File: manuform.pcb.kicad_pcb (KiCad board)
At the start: 2 copper layers, 84.5 x 93.5 mm, 100 parts, among them J1 Conn_01x01_Pin, J10 Conn_01x01_Pin, J11 Conn_01x01_Pin, J12 Conn_01x01_Pin, J2 Conn_01x01_Pin, J3 Conn_01x01, J4 Conn_01x01, J5 Conn_01x01_Pin, J6 Conn_01x01_Pin, J7 Conn_01x01_Pin, J8 Conn_01x01_Pin, J9 Conn_01x01_Pin, SW1 SW_DIP_x01, SW2 SW_DIP_x01, SW3 SW_DIP_x01, SW4 SW_DIP_x01

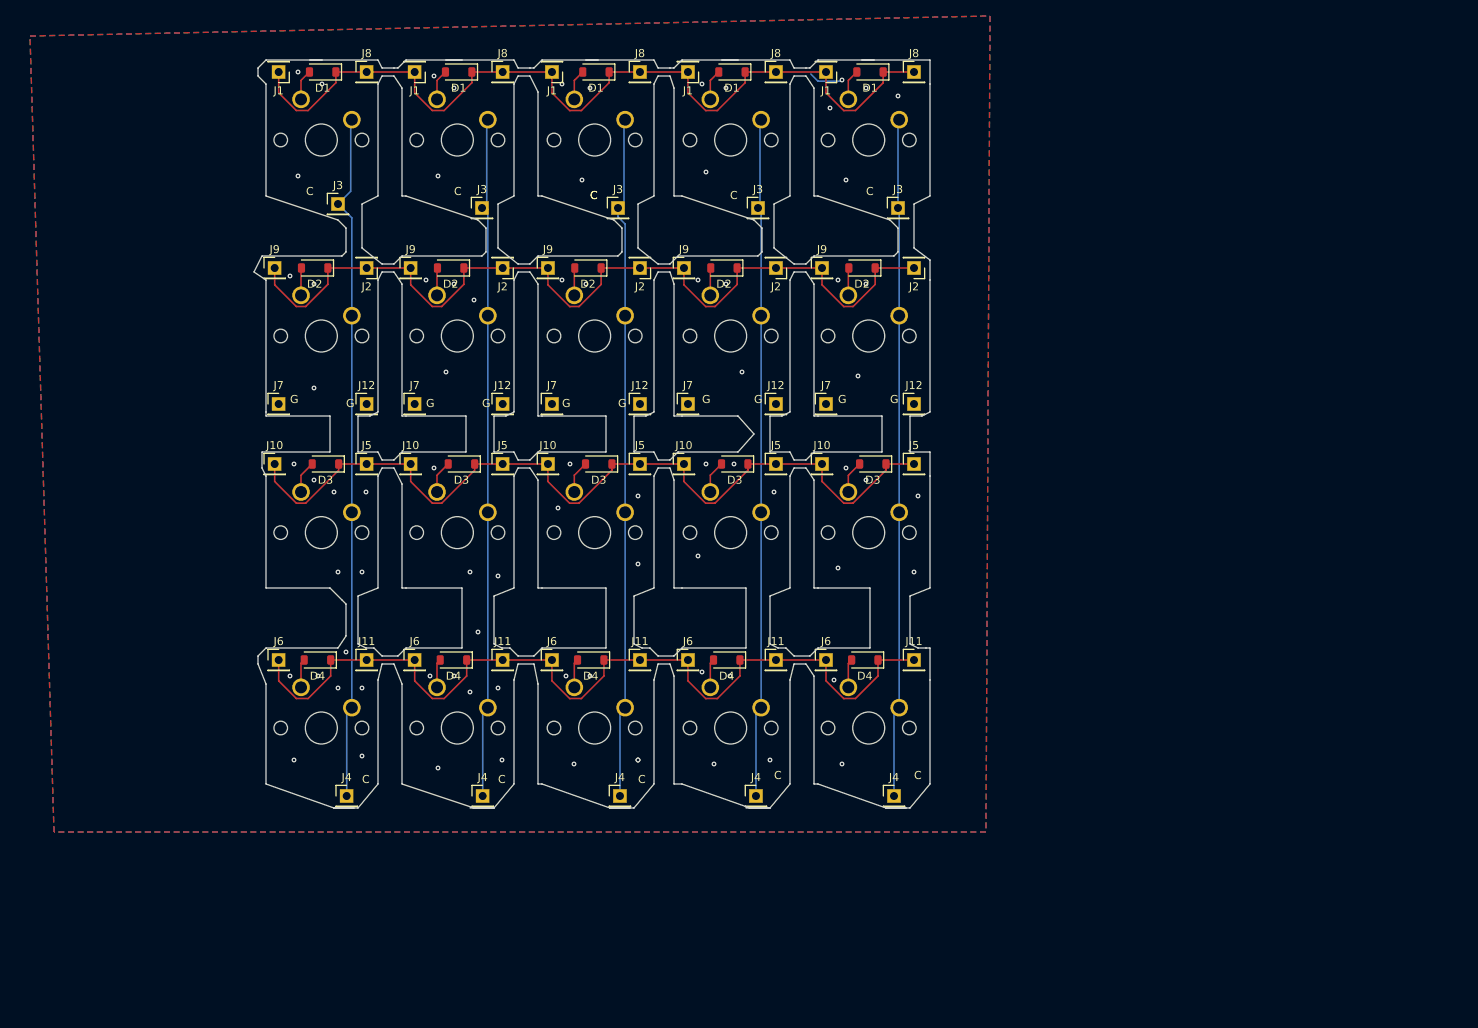
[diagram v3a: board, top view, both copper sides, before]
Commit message: new version with longer mehanical and solder holes.
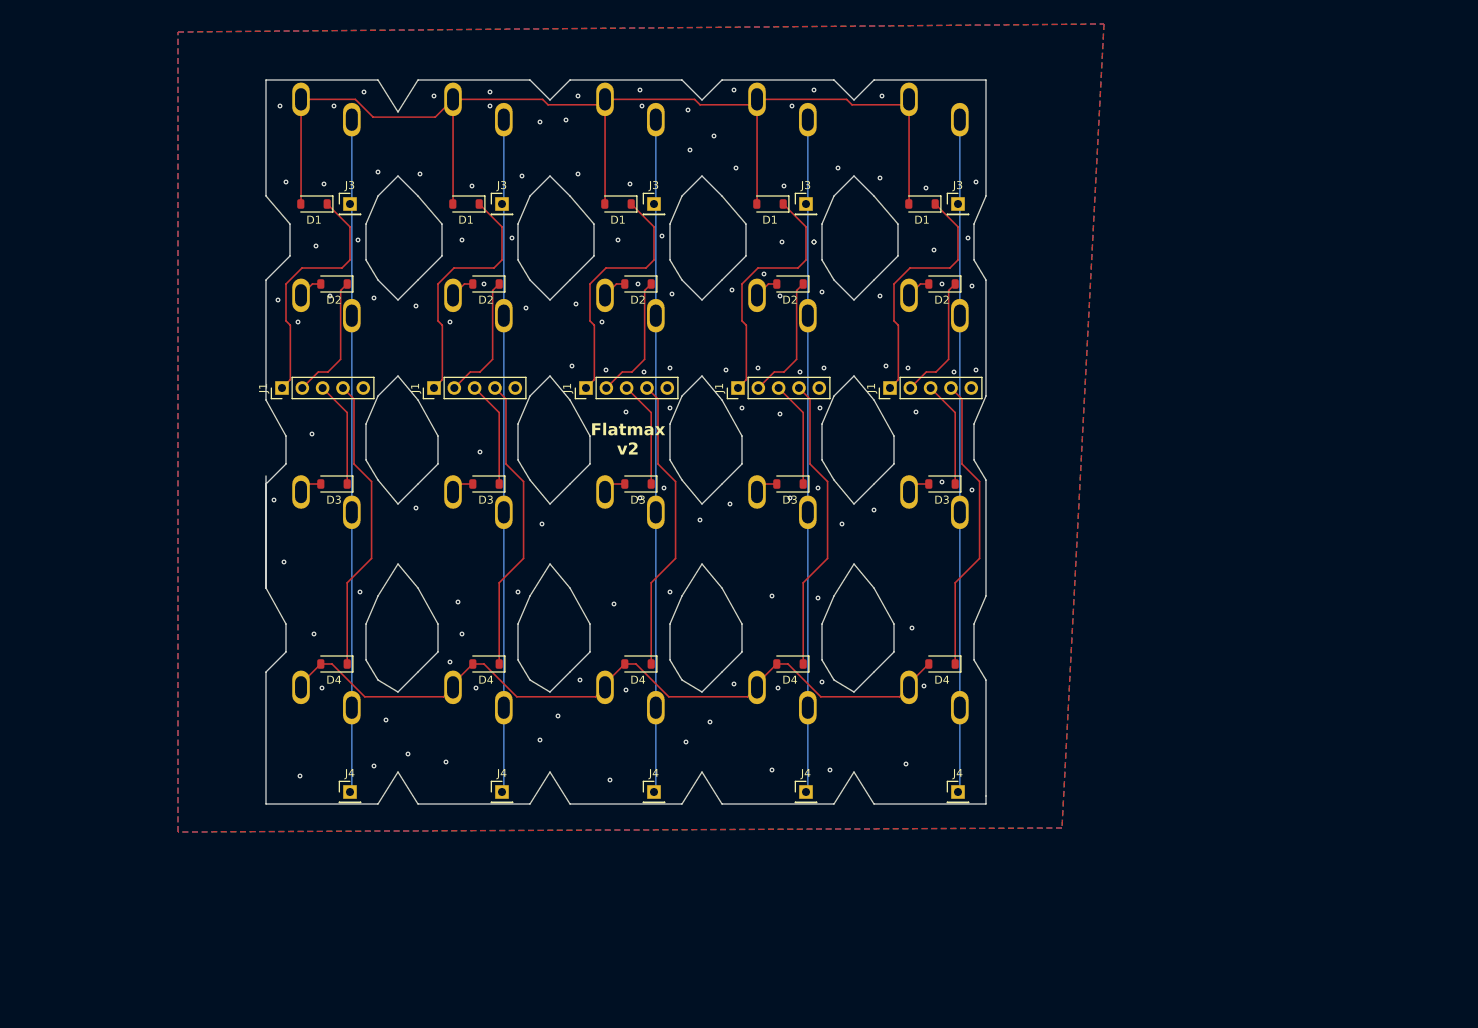
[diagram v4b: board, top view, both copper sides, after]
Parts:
- removed the D1 at (139.1, 16.5)
- removed the D1 at (156.2, 16.5)
- removed the D1 at (190.5, 16.5)
- removed the D1 at (173.2, 16.5)
- removed the D2 at (172.2, 41.0)
- removed the D2 at (138.1, 41.0)
- removed the D2 at (155.2, 41.0)
- removed the D2 at (189.5, 41.0)
- removed the D3 at (173.6, 65.5)
- removed the D3 at (139.4, 65.5)
- removed the D3 at (190.8, 65.5)
- removed the D3 at (156.6, 65.5)
- removed the D4 at (172.6, 90.0)
- removed the D4 at (138.4, 90.0)
- removed the D4 at (155.6, 90.0)
- removed the D4 at (189.8, 90.0)
- removed the J1 at (150.7, 16.5)
- removed the J1 at (185.0, 16.5)
- removed the J1 at (167.7, 16.5)
- removed the J1 at (133.6, 16.5)
- removed J10 (x5), J11 (x5), J12 (x5), J2 (x5), J5 (x5), J6 (x5), J7 (x5), J8 (x5), J9 (x5): Conn_01x01_Pin, Connector_PinHeader_2.54mm:PinHeader_1x01_P2.54mm_Vertical
- removed the J3 at (159.0, 33.5)
- removed the J3 at (142.0, 33.5)
- removed the J3 at (176.5, 33.5)
- removed the J3 at (194.0, 33.5)
- removed the J4 at (176.2, 107.0)
- removed the J4 at (159.2, 107.0)
- removed the J4 at (142.1, 107.0)
- removed the J4 at (193.5, 107.0)
- removed the SW1 at (153.5, 19.9)
- removed the SW1 at (136.4, 19.9)
- removed the SW1 at (187.8, 19.9)
- removed the SW1 at (170.5, 19.9)
- removed the SW2 at (136.4, 44.4)
- removed the SW2 at (170.5, 44.4)
- removed the SW2 at (187.8, 44.4)
- removed the SW2 at (153.5, 44.4)
- removed the SW3 at (187.8, 69.0)
- removed the SW3 at (136.4, 69.0)
- removed the SW3 at (170.5, 69.0)
- removed the SW3 at (153.5, 69.0)
- removed the SW4 at (170.5, 93.4)
- removed the SW4 at (153.5, 93.4)
- removed the SW4 at (187.8, 93.4)
- removed the SW4 at (136.4, 93.4)
- added D1: D, Diode_SMD:D_SOD-123, F.Cu at (178.0, 33.0)
- added D1: D, Diode_SMD:D_SOD-123, F.Cu at (159.0, 33.0)
- added D1: D, Diode_SMD:D_SOD-123, F.Cu at (197.0, 33.0)
- added D1: D, Diode_SMD:D_SOD-123, F.Cu at (140.0, 33.0)
- added D2: D, Diode_SMD:D_SOD-123, F.Cu at (199.5, 43.0)
- added D2: D, Diode_SMD:D_SOD-123, F.Cu at (142.5, 43.0)
- added D2: D, Diode_SMD:D_SOD-123, F.Cu at (180.5, 43.0)
- added D2: D, Diode_SMD:D_SOD-123, F.Cu at (161.5, 43.0)
- added D3: D, Diode_SMD:D_SOD-123, F.Cu at (199.5, 68.0)
- added D3: D, Diode_SMD:D_SOD-123, F.Cu at (180.5, 68.0)
- added D3: D, Diode_SMD:D_SOD-123, F.Cu at (142.5, 68.0)
- added D3: D, Diode_SMD:D_SOD-123, F.Cu at (161.5, 68.0)
- added D4: D, Diode_SMD:D_SOD-123, F.Cu at (199.5, 90.5)
- added D4: D, Diode_SMD:D_SOD-123, F.Cu at (180.5, 90.5)
- added D4: D, Diode_SMD:D_SOD-123, F.Cu at (142.5, 90.5)
- added D4: D, Diode_SMD:D_SOD-123, F.Cu at (161.5, 90.5)
- added J1: Conn_01x05, Connector_PinHeader_2.54mm:PinHeader_1x05_P2.54mm_Vertical, F.Cu at (193.0, 56.0)
- added J1: Conn_01x05, Connector_PinHeader_2.54mm:PinHeader_1x05_P2.54mm_Vertical, F.Cu at (155.0, 56.0)
- added J1: Conn_01x05, Connector_PinHeader_2.54mm:PinHeader_1x05_P2.54mm_Vertical, F.Cu at (136.0, 56.0)
- added J1: Conn_01x05, Connector_PinHeader_2.54mm:PinHeader_1x05_P2.54mm_Vertical, F.Cu at (174.0, 56.0)
- added J3: Conn_01x01, Connector_PinHeader_2.54mm:PinHeader_1x01_P2.54mm_Vertical, F.Cu at (163.5, 33.0)
- added J3: Conn_01x01, Connector_PinHeader_2.54mm:PinHeader_1x01_P2.54mm_Vertical, F.Cu at (182.5, 33.0)
- added J3: Conn_01x01, Connector_PinHeader_2.54mm:PinHeader_1x01_P2.54mm_Vertical, F.Cu at (144.5, 33.0)
- added J3: Conn_01x01, Connector_PinHeader_2.54mm:PinHeader_1x01_P2.54mm_Vertical, F.Cu at (201.5, 33.0)
- added J4: Conn_01x01, Connector_PinHeader_2.54mm:PinHeader_1x01_P2.54mm_Vertical, F.Cu at (163.5, 106.5)
- added J4: Conn_01x01, Connector_PinHeader_2.54mm:PinHeader_1x01_P2.54mm_Vertical, F.Cu at (201.5, 106.5)
- added J4: Conn_01x01, Connector_PinHeader_2.54mm:PinHeader_1x01_P2.54mm_Vertical, F.Cu at (182.5, 106.5)
- added J4: Conn_01x01, Connector_PinHeader_2.54mm:PinHeader_1x01_P2.54mm_Vertical, F.Cu at (144.5, 106.5)
- added SW1: SW_DIP_x01, switchCustom:SW_Cherry_MX_1.00u_PCB, B.Cu at (176.4, 19.9)
- added SW1: SW_DIP_x01, switchCustom:SW_Cherry_MX_1.00u_PCB, B.Cu at (157.4, 19.9)
- added SW1: SW_DIP_x01, switchCustom:SW_Cherry_MX_1.00u_PCB, B.Cu at (138.4, 19.9)
- added SW1: SW_DIP_x01, switchCustom:SW_Cherry_MX_1.00u_PCB, B.Cu at (195.4, 19.9)
- added SW2: SW_DIP_x01, switchCustom:SW_Cherry_MX_1.00u_PCB, B.Cu at (157.4, 44.4)
- added SW2: SW_DIP_x01, switchCustom:SW_Cherry_MX_1.00u_PCB, B.Cu at (195.4, 44.4)
- added SW2: SW_DIP_x01, switchCustom:SW_Cherry_MX_1.00u_PCB, B.Cu at (176.4, 44.4)
- added SW2: SW_DIP_x01, switchCustom:SW_Cherry_MX_1.00u_PCB, B.Cu at (138.4, 44.4)
- added SW3: SW_DIP_x01, switchCustom:SW_Cherry_MX_1.00u_PCB, B.Cu at (138.4, 69.0)
- added SW3: SW_DIP_x01, switchCustom:SW_Cherry_MX_1.00u_PCB, B.Cu at (195.4, 69.0)
- added SW3: SW_DIP_x01, switchCustom:SW_Cherry_MX_1.00u_PCB, B.Cu at (176.4, 69.0)
- added SW3: SW_DIP_x01, switchCustom:SW_Cherry_MX_1.00u_PCB, B.Cu at (157.4, 69.0)
- added SW4: SW_DIP_x01, switchCustom:SW_Cherry_MX_1.00u_PCB, B.Cu at (157.4, 93.4)
- added SW4: SW_DIP_x01, switchCustom:SW_Cherry_MX_1.00u_PCB, B.Cu at (138.4, 93.4)
- added SW4: SW_DIP_x01, switchCustom:SW_Cherry_MX_1.00u_PCB, B.Cu at (195.4, 93.4)
- added SW4: SW_DIP_x01, switchCustom:SW_Cherry_MX_1.00u_PCB, B.Cu at (176.4, 93.4)
- J1: value Conn_01x01_Pin -> Conn_01x05; footprint Connector_PinHeader_2.54mm:PinHeader_1x01_P2.54mm_Vertical -> Connector_PinHeader_2.54mm:PinHeader_1x05_P2.54mm_Vertical
- SW1, SW2, SW3, SW4: footprint Button_Switch_Keyboard:SW_Cherry_MX_1.00u_PCB -> switchCustom:SW_Cherry_MX_1.00u_PCB
- moved J1 39.5 mm to (117.0, 56.0), turned to 90 degrees
- moved D1 16.5 mm to (121.0, 33.0)
- moved D2 3.14 mm to (123.5, 43.0)
- moved D3 2.72 mm to (123.5, 68.0)
- moved D4 2.13 mm to (123.5, 90.5)
- moved J3 1.50 mm to (125.5, 33.0)
- moved J4 0.65 mm to (125.5, 106.5)
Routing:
- net Net-(D1-A): track 19.3 -> 145.0 mm
- net Net-(D4-A): track 17.9 -> 94.6 mm
- net Net-(D4-K): track 112.9 -> 186.2 mm
- net Net-(D1-K): track 111.0 -> 155.4 mm
- net Net-(D3-K): track 108.9 -> 66.4 mm
- net Net-(D2-K): track 112.0 -> 80.1 mm
- net Net-(D3-A): track 20.4 -> 14.4 mm
- net Net-(J3-Pin_1): track 426.3 -> 420.7 mm
- net GND: track 4.33 -> 0.00 mm, vias 79 -> 128
- net Net-(D2-A): track 17.2 -> 15.3 mm
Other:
- board size 84.5 x 93.5 mm -> 90 x 90.5 mm
- board text added: "Flatmax v2"
- board text removed: "C"
- board text removed: "G"

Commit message: kalih choc v2 flex PCB
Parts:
- removed D1 (x5), D2 (x5), D3 (x5), D4 (x5): D, Diode_SMD:D_SOD-123
- removed the J1 at (117.0, 56.0)
- removed the J1 at (193.0, 56.0)
- removed the J1 at (155.0, 56.0)
- removed the J1 at (136.0, 56.0)
- removed the J1 at (174.0, 56.0)
- removed the J3 at (125.5, 33.0)
- removed the J3 at (163.5, 33.0)
- removed the J3 at (182.5, 33.0)
- removed the J3 at (144.5, 33.0)
- removed the J3 at (201.5, 33.0)
- removed J4 (x5): Conn_01x01, Connector_PinHeader_2.54mm:PinHeader_1x01_P2.54mm_Vertical
- removed the SW1 at (119.4, 19.9)
- removed the SW1 at (176.4, 19.9)
- removed the SW1 at (157.4, 19.9)
- removed the SW1 at (138.4, 19.9)
- removed the SW1 at (195.4, 19.9)
- removed the SW2 at (119.4, 44.4)
- removed the SW2 at (157.4, 44.4)
- removed the SW2 at (195.4, 44.4)
- removed the SW2 at (176.4, 44.4)
- removed the SW2 at (138.4, 44.4)
- removed the SW3 at (138.4, 69.0)
- removed the SW3 at (195.4, 69.0)
- removed the SW3 at (119.4, 69.0)
- removed the SW3 at (176.4, 69.0)
- removed the SW3 at (157.4, 69.0)
- removed the SW4 at (119.4, 93.4)
- removed the SW4 at (157.4, 93.4)
- removed the SW4 at (138.4, 93.4)
- removed the SW4 at (195.4, 93.4)
- removed the SW4 at (176.4, 93.4)
- added J1: Conn_01x04, Connector_PinHeader_2.00mm:PinHeader_1x04_P2.00mm_Horizontal, F.Cu at (183.5, 75.9)
- added J1: Conn_01x04, Connector_PinHeader_2.00mm:PinHeader_1x04_P2.00mm_Horizontal, F.Cu at (217.5, 75.9)
- added J1: Conn_01x04, Connector_PinHeader_2.00mm:PinHeader_1x04_P2.00mm_Horizontal, F.Cu at (234.5, 75.9)
- added J1: Conn_01x04, Connector_PinHeader_2.00mm:PinHeader_1x04_P2.00mm_Horizontal, F.Cu at (251.5, 75.9)
- added J1: Conn_01x04, Connector_PinHeader_2.00mm:PinHeader_1x04_P2.00mm_Horizontal, F.Cu at (166.5, 75.9)
- added J1: Conn_01x04, Connector_PinHeader_2.00mm:PinHeader_1x04_P2.00mm_Horizontal, F.Cu at (200.5, 75.9)
- added J2: Conn_01x04, Connector_PinHeader_2.00mm:PinHeader_1x04_P2.00mm_Vertical, F.Cu at (216.9, 46.0)
- added J2: Conn_01x04, Connector_PinHeader_2.00mm:PinHeader_1x04_P2.00mm_Vertical, F.Cu at (250.9, 46.0)
- added J2: Conn_01x04, Connector_PinHeader_2.00mm:PinHeader_1x04_P2.00mm_Vertical, F.Cu at (182.9, 46.0)
- added J2: Conn_01x04, Connector_PinHeader_2.00mm:PinHeader_1x04_P2.00mm_Vertical, F.Cu at (165.9, 46.0)
- added J2: Conn_01x04, Connector_PinHeader_2.00mm:PinHeader_1x04_P2.00mm_Vertical, F.Cu at (233.9, 46.0)
- added J2: Conn_01x04, Connector_PinHeader_2.00mm:PinHeader_1x04_P2.00mm_Vertical, F.Cu at (199.9, 46.0)
- added J3: Conn_01x04, Connector_PinHeader_2.00mm:PinHeader_1x04_P2.00mm_Vertical, F.Cu at (240.1, 95.5)
- added J3: Conn_01x04, Connector_PinHeader_2.00mm:PinHeader_1x04_P2.00mm_Vertical, F.Cu at (155.1, 95.5)
- added J3: Conn_01x04, Connector_PinHeader_2.00mm:PinHeader_1x04_P2.00mm_Vertical, F.Cu at (223.1, 95.5)
- added J3: Conn_01x04, Connector_PinHeader_2.00mm:PinHeader_1x04_P2.00mm_Vertical, F.Cu at (206.1, 95.5)
- added J3: Conn_01x04, Connector_PinHeader_2.00mm:PinHeader_1x04_P2.00mm_Vertical, F.Cu at (172.1, 95.5)
- added J3: Conn_01x04, Connector_PinHeader_2.00mm:PinHeader_1x04_P2.00mm_Vertical, F.Cu at (189.1, 95.5)
- added JP1: SolderJumper_3_Open, Jumper:SolderJumper-3_P2.0mm_Open_TrianglePad1.0x1.5mm_NumberLabels, F.Cu at (251.2, 98.2)
- added JP1: SolderJumper_3_Open, Jumper:SolderJumper-3_P2.0mm_Open_TrianglePad1.0x1.5mm_NumberLabels, F.Cu at (217.2, 98.3)
- added JP1: SolderJumper_3_Open, Jumper:SolderJumper-3_P2.0mm_Open_TrianglePad1.0x1.5mm_NumberLabels, F.Cu at (166.0, 98.2)
- added JP1: SolderJumper_3_Open, Jumper:SolderJumper-3_P2.0mm_Open_TrianglePad1.0x1.5mm_NumberLabels, F.Cu at (234.2, 98.3)
- added JP1: SolderJumper_3_Open, Jumper:SolderJumper-3_P2.0mm_Open_TrianglePad1.0x1.5mm_NumberLabels, F.Cu at (200.2, 98.2)
- added JP1: SolderJumper_3_Open, Jumper:SolderJumper-3_P2.0mm_Open_TrianglePad1.0x1.5mm_NumberLabels, F.Cu at (183.2, 98.2)
- added SW1: SW_DIP_x01, switchCustom:SW_Kailh_Choc_V2_elongated, F.Cu at (246.2, 45.5)
- added SW1: SW_DIP_x01, switchCustom:SW_Kailh_Choc_V2_elongated, F.Cu at (229.2, 45.5)
- added SW1: SW_DIP_x01, switchCustom:SW_Kailh_Choc_V2_elongated, F.Cu at (195.2, 45.5)
- added SW1: SW_DIP_x01, switchCustom:SW_Kailh_Choc_V2_elongated, F.Cu at (161.2, 45.5)
- added SW1: SW_DIP_x01, switchCustom:SW_Kailh_Choc_V2_elongated, F.Cu at (178.2, 45.5)
- added SW1: SW_DIP_x01, switchCustom:SW_Kailh_Choc_V2_elongated, F.Cu at (212.2, 45.5)
- added SW2: SW_DIP_x01, switchCustom:SW_Kailh_Choc_V2_elongated, F.Cu at (195.2, 70.0)
- added SW2: SW_DIP_x01, switchCustom:SW_Kailh_Choc_V2_elongated, F.Cu at (246.2, 70.0)
- added SW2: SW_DIP_x01, switchCustom:SW_Kailh_Choc_V2_elongated, F.Cu at (178.2, 70.0)
- added SW2: SW_DIP_x01, switchCustom:SW_Kailh_Choc_V2_elongated, F.Cu at (229.2, 70.0)
- added SW2: SW_DIP_x01, switchCustom:SW_Kailh_Choc_V2_elongated, F.Cu at (161.2, 70.0)
- added SW2: SW_DIP_x01, switchCustom:SW_Kailh_Choc_V2_elongated, F.Cu at (212.2, 70.0)
- added SW3: SW_DIP_x01, switchCustom:SW_Kailh_Choc_V2_elongated, F.Cu at (178.1, 94.5)
- added SW3: SW_DIP_x01, switchCustom:SW_Kailh_Choc_V2_elongated, F.Cu at (229.1, 94.5)
- added SW3: SW_DIP_x01, switchCustom:SW_Kailh_Choc_V2_elongated, F.Cu at (212.1, 94.5)
- added SW3: SW_DIP_x01, switchCustom:SW_Kailh_Choc_V2_elongated, F.Cu at (195.1, 94.5)
- added SW3: SW_DIP_x01, switchCustom:SW_Kailh_Choc_V2_elongated, F.Cu at (161.1, 94.5)
- added SW3: SW_DIP_x01, switchCustom:SW_Kailh_Choc_V2_elongated, F.Cu at (246.1, 94.5)
- added SW4: SW_DIP_x01, switchCustom:SW_Kailh_Choc_V2_elongated, F.Cu at (178.0, 119.0)
- added SW4: SW_DIP_x01, switchCustom:SW_Kailh_Choc_V2_elongated, F.Cu at (161.0, 119.0)
- added SW4: SW_DIP_x01, switchCustom:SW_Kailh_Choc_V2_elongated, F.Cu at (212.0, 119.0)
- added SW4: SW_DIP_x01, switchCustom:SW_Kailh_Choc_V2_elongated, F.Cu at (246.0, 119.0)
- added SW4: SW_DIP_x01, switchCustom:SW_Kailh_Choc_V2_elongated, F.Cu at (229.0, 119.0)
- added SW4: SW_DIP_x01, switchCustom:SW_Kailh_Choc_V2_elongated, F.Cu at (195.0, 119.0)
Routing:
- net Net-(J3-Pin_1): track 420.7 -> 0.00 mm
- net Net-(J1-Pin_1): track 0.00 -> 230.9 mm
- net Net-(D4-K): track 186.2 -> 0.00 mm
- net Net-(D1-K): track 155.4 -> 0.00 mm
- net Net-(D1-A): track 145.0 -> 0.00 mm
- net Net-(J1-Pin_3): track 0.00 -> 143.4 mm
- net Net-(D4-A): track 94.6 -> 0.00 mm
- net Net-(JP1-B): track 0.00 -> 90.4 mm
- net Net-(D2-K): track 80.1 -> 0.00 mm
- net Net-(J1-Pin_2): track 0.00 -> 79.0 mm
- net Net-(J1-Pin_4): track 0.00 -> 77.7 mm
- net Net-(D3-K): track 66.4 -> 0.00 mm
- net Net-(D2-A): track 15.3 -> 0.00 mm
- net Net-(D3-A): track 14.4 -> 0.00 mm
- net GND: vias 128 -> 29
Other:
- board size 90 x 90.5 mm -> 100 x 90 mm
- board text added: "Choc v2"
- board text added: "Flatmax v1.0"
- board text added: "GND"
- board text added: "SW"
- board text removed: "Flatmax v2"
